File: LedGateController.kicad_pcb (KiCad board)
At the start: 2 copper layers, 49 parts, among them J1 GPIO, J2 SWD, J3 LED_OUT, Q1 FS8205A, Q2 AO3400A, Q3 AO3401A, SW1 BUTTON, SW2 ON_OFF, U1 STM32F030F4Px, U2 MT3608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

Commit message: nearly done
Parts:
- added ?: MountingHole_3.2mm_M3_ISO7380, MountingHole:MountingHole_3.2mm_M3_ISO7380, F.Cu at (161.8, 23.2)
- added ?: MountingHole_3.2mm_M3_ISO7380, MountingHole:MountingHole_3.2mm_M3_ISO7380, F.Cu at (23.2, 41.8)
- added ?: MountingHole_3.2mm_M3_ISO7380, MountingHole:MountingHole_3.2mm_M3_ISO7380, F.Cu at (23.2, 23.2)
- J1: footprint Connector_PinHeader_2.54mm:PinHeader_1x10_P2.54mm_Vertical -> Connector_PinHeader_2.54mm:PinHeader_1x06_P2.54mm_Vertical
- SW1: footprint Button_Switch_THT:SW_PUSH_6mm -> LedGateController:TS-1009B-04326
- SW2: footprint Button_Switch_THT:SW_CuK_OS102011MA1QN1_SPDT_Angled -> SamacSys_Parts:SK12D07VG4NSPA
- TP1, TP2, TP3, TP4, TP5, TP6, TP7: footprint TestPoint:TestPoint_THTPad_D2.0mm_Drill1.0mm -> TestPoint:TestPoint_THTPad_D1.5mm_Drill0.7mm
- moved SW2 90.7 mm to (117.0, 22.2), turned to 180 degrees
- moved C2 89.6 mm to (128.2, 29.6), turned to 90 degrees
- moved U2 82.0 mm to (129.0, 33.9), turned to 90 degrees
- moved R2 80.4 mm to (145.6, 31.6), turned to 270 degrees
- moved C3 80.0 mm to (143.8, 27.2), turned to 90 degrees
- moved C8 76.3 mm to (139.7, 27.2), turned to 90 degrees
- moved R10 75.0 mm to (134.2, 26.3)
- moved C7 74.9 mm to (141.7, 27.3), turned to 90 degrees
- moved D2 74.7 mm to (117.9, 26.6), turned to 0 degrees
- moved R7 74.4 mm to (107.2, 26.1), turned to 90 degrees
- moved Q3 72.5 mm to (109.9, 27.3)
- moved R9 72.0 mm to (131.3, 25.4), turned to 0 degrees
- moved L1 71.2 mm to (121.7, 33.5), turned to 270 degrees
- moved R8 70.8 mm to (121.6, 26.6), turned to 180 degrees
- moved TP7 69.4 mm to (133.5, 29.9)
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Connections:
- J1 pad 1: /PA3 -> GND
- J1 pad 2: /PA4 -> /PA2
- J1 pad 3: /PA5 -> /PA1
- J1 pad 4: /PA6 -> /PA5
- J1 pad 5: /PA7 -> /PA6
- J1 pad 6: /PA10 -> +3V3
- U1 pad 10: /PA4 -> /BATT_ADC
- U1 pad 13: /PA7 -> Net-(U1-Pad13)
- U1 pad 17: /LED_DATA_3V3 -> Net-(U1-Pad17)
- U1 pad 18: /PA10 -> /LED_DATA_3V3
- U1 pad 6: /BATT_ADC -> /LED_EN
- U1 pad 7: /BUTTON -> /PA1
- U1 pad 8: /LED_EN -> /PA2
- U1 pad 9: /PA3 -> /BUTTON
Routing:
- net +BATT: track 0.00 -> 86.1 mm
- net +3V3: track 0.00 -> 83.3 mm, vias 0 -> 4
- net +5V: track 0.00 -> 56.5 mm
- net GND: track 0.00 -> 41.3 mm, vias 0 -> 37
- net +BATT_SW: track 0.00 -> 29.5 mm
- net Net-(BT1-Pad2): track 0.00 -> 27.2 mm
- net /LED_EN: track 0.00 -> 27.2 mm, vias 0 -> 2
- net /LED_DATA_3V3: track 0.00 -> 25.0 mm, vias 0 -> 2
- net /BUTTON: track 0.00 -> 19.0 mm
- net /SWDCLK: track 0.00 -> 19.0 mm, vias 0 -> 1
- net /SWDIO: track 0.00 -> 18.1 mm, vias 0 -> 1
- net /PA5: track 0.00 -> 17.2 mm, vias 0 -> 1
- net /LED_DATA_5V: track 0.00 -> 16.6 mm, vias 0 -> 1
- net /PA6: track 0.00 -> 16.3 mm, vias 0 -> 1
- net /PA2: track 0.00 -> 16.1 mm, vias 0 -> 1
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- added copper zone on F.Cu, net +5V
- added copper zone on F.Cu, net +BATT
- added copper zone on F.Cu, net +BATT_SW
- added copper zone on B.Cu, net GND
- added copper zone on F.Cu, net GND
- added copper zone on F.Cu, net Net-(BT1-Pad2)
- added copper zone on F.Cu, net Net-(D1-Pad2)
- added copper zone on F.Cu, net Net-(Q1-Pad1)
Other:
- board outline added: 145 x 25 mm
- net class Default: clearance 0.2 -> 0.15; via_drill 0.4 -> 0.6
- net class Power (Main) added: clearance 0.15, trace_width 2, via_dia 2, via_drill 1.7
- rule trace_clearance: 0.2 -> 0.15
- rule trace_min: 0.2 -> 0.15
- rule via_min_drill: 0.3 -> 0.35
- rule via_min_size: 0.4 -> 0.7

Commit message: Rev. 1 nearly ready!
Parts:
- moved R6 14.8 mm to (150.5, 28.0), turned to 0 degrees
- moved Q2 11.2 mm to (150.4, 30.8)
- moved R4 8.55 mm to (132.8, 34.8), turned to 180 degrees
- moved R3 7.12 mm to (132.8, 32.8), turned to 180 degrees
- moved R9 6.03 mm to (125.5, 26.6)
- moved R10 4.99 mm to (129.2, 26.6), turned to 0 degrees
- moved C12 4.56 mm to (157.0, 29.5)
- moved C14 4.55 mm to (157.0, 31.5)
- moved U5 4.27 mm to (160.8, 32.0)
- moved TP6 3.80 mm to (163.4, 27.9)
- moved TP5 2.84 mm to (160.4, 27.6)
- moved C11 2.82 mm to (133.9, 40.5), turned to 270 degrees
- moved TP3 2.48 mm to (132.1, 37.2)
- moved C10 2.04 mm to (128.3, 40.5)
- moved U4 1.90 mm to (131.1, 40.6)
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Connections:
- J1 pad 2: /PA2 -> +3V3
- J1 pad 3: /PA1 -> /PA2
- J1 pad 4: /PA5 -> /PA1
- J1 pad 5: /PA6 -> /PA5
- J1 pad 6: +3V3 -> /PA6
- J2 pad 2: /NRST -> +3V3
- J2 pad 3: /SWDIO -> /NRST
- J2 pad 4: /SWDCLK -> /SWDIO
- J2 pad 5: +3V3 -> /SWDCLK
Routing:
- net GND: track 41.3 -> 17.8 mm, vias 37 -> 27
- net +BATT_SW: track 29.5 -> 12.2 mm
- net /LED_EN: track 27.2 -> 13.9 mm
- net /LED_DATA_3V3: track 25.0 -> 32.5 mm, vias 2 -> 1
- net /SWDCLK: track 19.0 -> 24.0 mm
- net /SWDIO: track 18.1 -> 22.9 mm
- net Net-(R3-Pad1): track 11.6 -> 7.43 mm, vias 2 -> 0
- net /BATT_ADC: track 12.1 -> 15.7 mm, vias 0 -> 1
- net /BUTTON: track 19.0 -> 16.7 mm, vias 0 -> 1
- net +5V: track 56.5 -> 58.8 mm, vias 0 -> 3
- net /PA2: track 16.1 -> 14.1 mm
- net /PA6: track 16.3 -> 17.6 mm
- net Net-(C13-Pad2): track 11.7 -> 12.9 mm
- net /PA1: track 14.1 -> 13.1 mm
- net Net-(Q2-Pad1): track 2.68 -> 1.88 mm
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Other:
- board size 145 x 25 mm -> 144.5 x 25 mm
- rule pad_to_mask_clearance: 0.051 -> 0.0508
- board text added: "3V3"
- board text added: "5V (<1A)"
- board text added: "CLK"
- board text added: "DATA"
- board text added: "GND"
- board text added: "IO"
- board text added: "JLCJLCJLCJLC"
- board text added: "NRST"
- board text added: "PA1"
- board text added: "PA2"
- board text added: "PA5"
- board text added: "PA6"
- board text added: "WS28xx LED Driver Rev. 1 github.com/knifa"

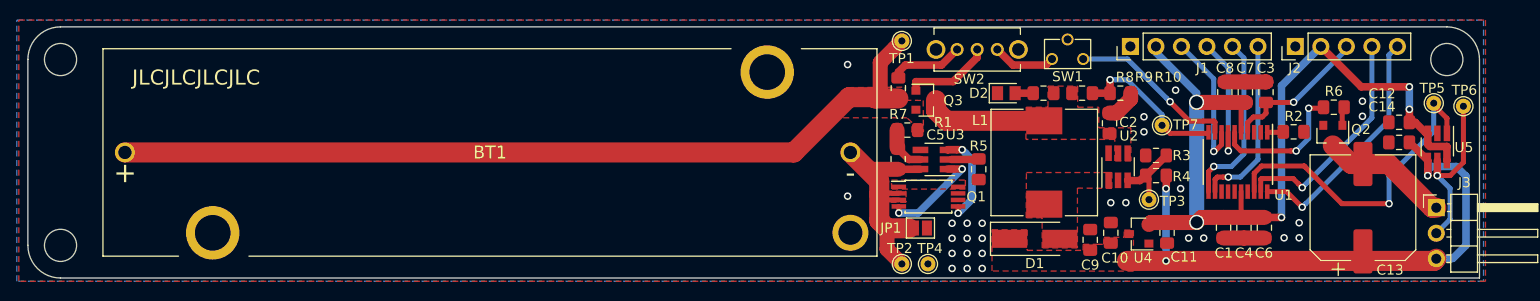
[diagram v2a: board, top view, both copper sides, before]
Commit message: Fix inductor schematic
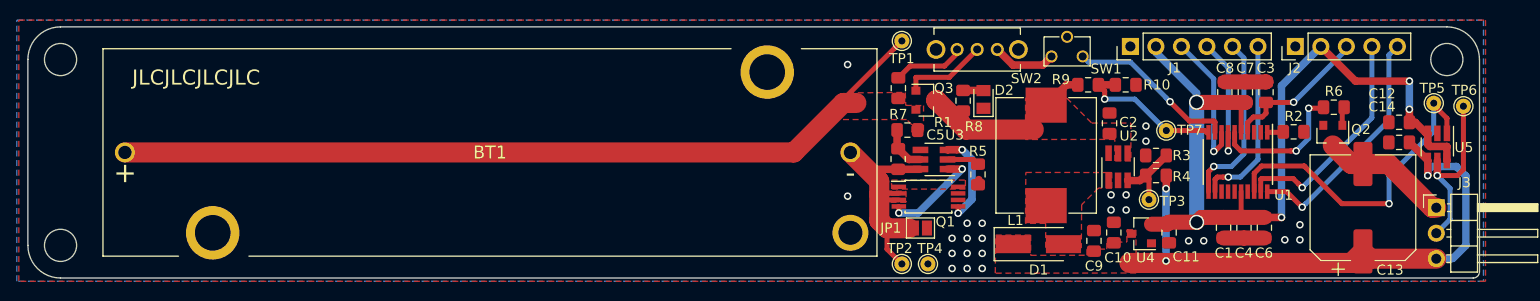
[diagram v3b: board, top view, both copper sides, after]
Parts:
- L1: footprint Inductor_SMD:L_10.4x10.4_H4.8 -> LedGateController:YT1040-220M
- moved R8 8.04 mm to (113.6, 27.4), turned to 90 degrees
- moved D2 2.36 mm to (115.6, 27.2), turned to 90 degrees
- moved R9 1.02 mm to (126.0, 25.8)
- moved R10 0.98 mm to (129.8, 25.8)
- moved L1 0.73 mm to (121.9, 32.8)
- moved TP7 0.68 mm to (133.8, 30.3)
- moved D1 0.64 mm to (121.1, 41.6)
- moved R5 0.52 mm to (115.1, 34.7)
- moved C9 0.39 mm to (126.6, 41.3)
- moved C10 0.30 mm to (128.6, 40.5)
- moved SW1 0.26 mm to (124.0, 22.2)
- moved U4 0.26 mm to (131.3, 40.6)
- moved C11 0.20 mm to (134.1, 40.5)
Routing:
- net +BATT_SW: track 12.2 -> 16.9 mm
- net GND: track 17.8 -> 15.1 mm, vias 27 -> 24
- net +BATT: track 86.1 -> 83.4 mm
- net /BATT_ADC: track 15.7 -> 15.0 mm
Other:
- outline, holes or cut-outs redrawn
- board text added: "5V"
- board text removed: "5V (<1A)"

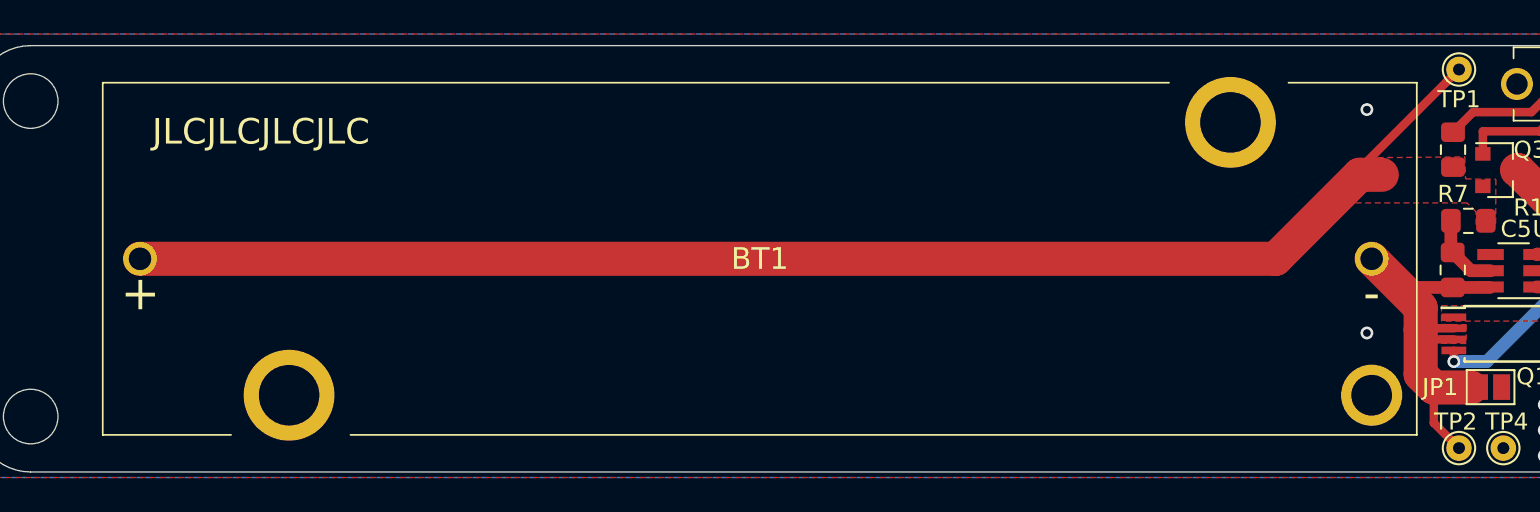
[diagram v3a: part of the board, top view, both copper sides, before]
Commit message: Fix battery orientation
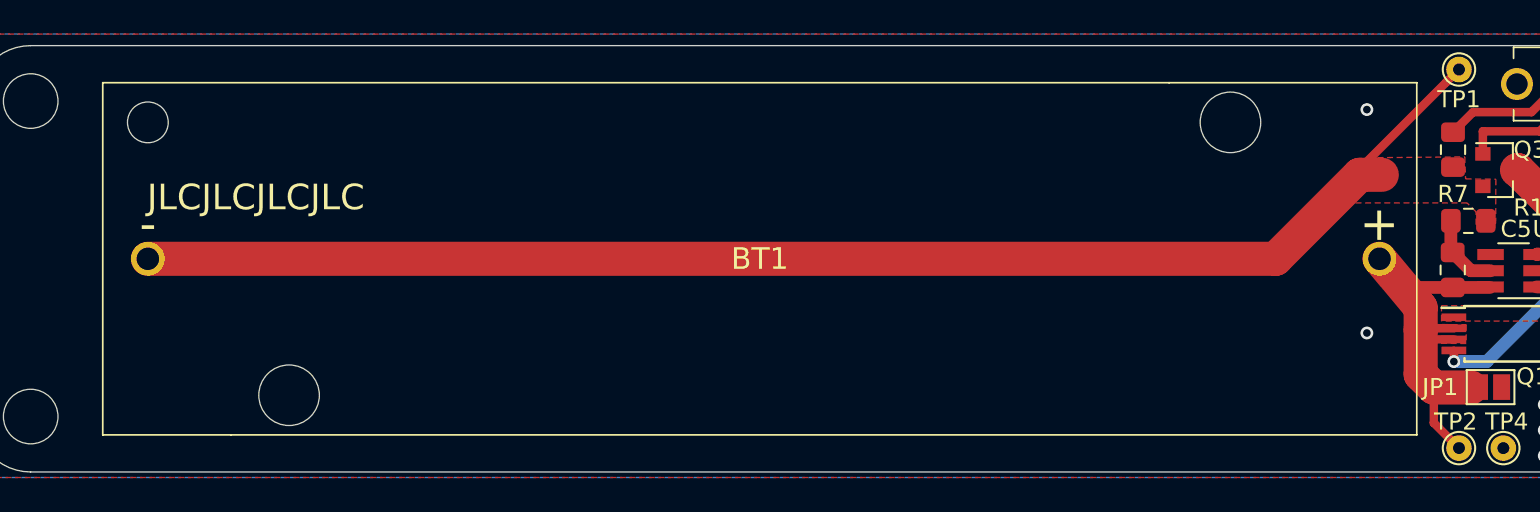
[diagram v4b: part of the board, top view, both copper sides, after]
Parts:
- turned BT1 to 180 degrees
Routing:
- net Net-(BT1-Pad2): track 27.2 -> 24.5 mm
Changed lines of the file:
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@@
     (thickness 1.6)
     (drawings 24)
-    (tracks 300)
+    (tracks 299)
     (zones 0)
     (modules 52)
@@
   )
   (setup
-    (last_trace_width 0.75)
+    (last_trace_width 0.25)
     (user_trace_width 0.5)
     (user_trace_width 0.75)
@@
     (add_net "Net-(C13-Pad2)")
   )
+  (module SamacSys_Parts:1043P (layer F.Cu)
+    (at 66.5 32.5 180)
+    (descr 1043P)
+    (tags "Undefined or Miscellaneous")
+    (fp_text reference BT1 (at 0 0) (layer F.SilkS)
+      (effects (font (size 1.27 1.27) (thickness 0.254)))
+    )
+    (fp_text value LI_ON (at 0 0) (layer F.SilkS) hide
+      (effects (font (size 1 1) (thickness 0.15)))
+    )
+    (fp_line (start 38.525 10.325) (end -24 10.325) (layer F.SilkS) (width 0.1))
+    (fp_line (start 38.525 -10.325) (end 38.525 10.325) (layer F.SilkS) (width 0.1))
+    (fp_line (start 31 -10.325) (end 38.525 -10.325) (layer F.SilkS) (width 0.1))
+    (fp_line (start -38.525 -10.325) (end 31 -10.325) (layer F.SilkS) (width 0.1))
+    (fp_line (start -38.525 10.325) (end -38.525 -10.325) (layer F.SilkS) (width 0.1))
+    (fp_line (start -24 10.325) (end -38.525 10.325) (layer F.SilkS) (width 0.1))
+    (fp_line (start -39.525 11.662) (end -39.525 -11.662) (layer F.CrtYd) (width 0.1))
+    (fp_line (start 39.525 11.662) (end -39.525 11.662) (layer F.CrtYd) (width 0.1))
+    (fp_line (start 39.525 -11.662) (end 39.525 11.662) (layer F.CrtYd) (width 0.1))
+    (fp_line (start -39.525 -11.662) (end 39.525 -11.662) (layer F.CrtYd) (width 0.1))
+    (fp_line (start -38.525 10.325) (end -38.525 -10.325) (layer F.Fab) (width 0.2))
+    (fp_line (start 38.525 10.325) (end -38.525 10.325) (layer F.Fab) (width 0.2))
+    (fp_line (start 38.525 -10.325) (end 38.525 10.325) (layer F.Fab) (width 0.2))
+    (fp_line (start -38.525 -10.325) (end 38.525 -10.325) (layer F.Fab) (width 0.2))
+    (fp_text user %R (at 0 0) (layer F.Fab)
+      (effects (font (size 1.27 1.27) (thickness 0.254)))
+    )
+    (fp_text user + (at -36.322 2.032 180) (layer F.SilkS)
+      (effects (font (size 2 2) (thickness 0.3)))
+    )
+    (fp_text user - (at 35.8775 2.032 180) (layer F.SilkS)
+      (effects (font (size 2 2) (thickness 0.3)))
+    )
+    (pad "" np_thru_hole circle (at -27.6 8 180) (size 3.55 3.55) (drill 3.55) (layers *.Cu *.Mask))
+    (pad "" np_thru_hole circle (at 35.88 8 180) (size 2.39 2.39) (drill 2.39) (layers *.Cu *.Mask))
+    (pad "" np_thru_hole circle (at 27.6 -8 180) (size 3.55 3.55) (drill 3.55) (layers *.Cu *.Mask))
+    (pad 1 thru_hole circle (at 35.88 0 180) (size 1.98 1.98) (drill 1.32) (layers *.Cu *.Mask)
+      (net 1 +BATT))
+    (pad 2 thru_hole circle (at -36.34 0 180) (size 1.98 1.98) (drill 1.32) (layers *.Cu *.Mask)
+      (net 2 "Net-(BT1-Pad2)"))
+    (model D:\Documents\Electronics\LibraryLoaderLibs\SamacSys_Parts.3dshapes\1043P.stp
+      (at (xyz 0 0 0))
+      (scale (xyz 1 1 1))
+      (rotate (xyz 0 0 0))
+    )
+  )
   (module LedGateController:YT1040-220M (layer F.Cu)
     (at 121.865 32.795 270)
@@
     )
     (pad 1 np_thru_hole circle (at 0 0) (size 3.2 3.2) (drill 3.2) (layers *.Cu *.Mask))
-  )
-  (module SamacSys_Parts:1043P (layer F.Cu)
-    (at 66.5 32.5)
-    (descr 1043P)
-    (tags "Undefined or Miscellaneous")
-    (fp_text reference BT1 (at 0 0) (layer F.SilkS)
-      (effects (font (size 1.27 1.27) (thickness 0.254)))
-    )
-    (fp_text value LI_ON (at 0 0) (layer F.SilkS) hide
-      (effects (font (size 1 1) (thickness 0.15)))
-    )
-    (fp_line (start 38.525 10.325) (end -24 10.325) (layer F.SilkS) (width 0.1))
-    (fp_line (start 38.525 -10.325) (end 38.525 10.325) (layer F.SilkS) (width 0.1))
-    (fp_line (start 31 -10.325) (end 38.525 -10.325) (layer F.SilkS) (width 0.1))
-    (fp_line (start -38.525 -10.325) (end 24 -10.325) (layer F.SilkS) (width 0.1))
-    (fp_line (start -38.525 10.325) (end -38.525 -10.325) (layer F.SilkS) (width 0.1))
-    (fp_line (start -31 10.325) (end -38.525 10.325) (layer F.SilkS) (width 0.1))
-    (fp_line (start -39.525 11.662) (end -39.525 -11.662) (layer F.CrtYd) (width 0.1))
-    (fp_line (start 39.525 11.662) (end -39.525 11.662) (layer F.CrtYd) (width 0.1))
-    (fp_line (start 39.525 -11.662) (end 39.525 11.662) (layer F.CrtYd) (width 0.1))
-    (fp_line (start -39.525 -11.662) (end 39.525 -11.662) (layer F.CrtYd) (width 0.1))
-    (fp_line (start -38.525 10.325) (end -38.525 -10.325) (layer F.Fab) (width 0.2))
-    (fp_line (start 38.525 10.325) (end -38.525 10.325) (layer F.Fab) (width 0.2))
-    (fp_line (start 38.525 -10.325) (end 38.525 10.325) (layer F.Fab) (width 0.2))
-    (fp_line (start -38.525 -10.325) (end 38.525 -10.325) (layer F.Fab) (width 0.2))
-    (fp_text user %R (at 0 0) (layer F.Fab)
-      (effects (font (size 1.27 1.27) (thickness 0.254)))
-    )
-    (fp_text user + (at -36.322 2.032) (layer F.SilkS)
-      (effects (font (size 2 2) (thickness 0.3)))
-    )
-    (fp_text user - (at 35.8775 2.032) (layer F.SilkS)
-      (effects (font (size 2 2) (thickness 0.3)))
-    )
-    (pad 5 thru_hole circle (at -27.6 8) (size 5.325 5.325) (drill 3.55) (layers *.Cu *.Mask))
-    (pad 4 thru_hole circle (at 35.88 8) (size 3.585 3.585) (drill 2.39) (layers *.Cu *.Mask))
-    (pad 3 thru_hole circle (at 27.6 -8) (size 5.325 5.325) (drill 3.55) (layers *.Cu *.Mask))
-    (pad 2 thru_hole circle (at 35.88 0) (size 1.98 1.98) (drill 1.32) (layers *.Cu *.Mask)
-      (net 2 "Net-(BT1-Pad2)"))
-    (pad 1 thru_hole circle (at -36.34 0) (size 1.98 1.98) (drill 1.32) (layers *.Cu *.Mask)
-      (net 1 +BATT))
-    (model D:\Documents\Electronics\LibraryLoaderLibs\SamacSys_Parts.3dshapes\1043P.stp
-      (at (xyz 0 0 0))
-      (scale (xyz 1 1 1))
-      (rotate (xyz 0 0 0))
-    )
   )
   (module Capacitor_SMD:C_0805_2012Metric_Pad1.15x1.40mm_HandSolder (layer F.Cu)
@@
   )
   (gr_arc (start 164.375 44.375) (end 164.375 45) (angle -90) (layer Edge.Cuts) (width 0.05))
-  (gr_text JLCJLCJLCJLC (at 37.25 25.05) (layer F.SilkS)
+  (gr_text JLCJLCJLCJLC (at 36.95 28.9) (layer F.SilkS)
     (effects (font (size 1.5 1.5) (thickness 0.3)))
   )
@@
   (gr_line (start 20.5 23.25) (end 20.5 41.75) (layer Edge.Cuts) (width 0.05))
   (segment (start 101.675 27.575) (end 102.975 27.575) (width 2) (layer F.Cu) (net 1))
-  (segment (start 30.16 32.5) (end 96.75 32.5) (width 2) (layer F.Cu) (net 1))
-  (segment (start 96.75 32.5) (end 101.675 27.575) (width 2) (layer F.Cu) (net 1))
   (segment (start 106.750001 22.149999) (end 107.5 21.4) (width 0.5) (layer F.Cu) (net 1))
   (segment (start 101.675 27.575) (end 101.675 27.225) (width 0.5) (layer F.Cu) (net 1))
   (segment (start 101.675 27.225) (end 106.750001 22.149999) (width 0.5) (layer F.Cu) (net 1))
+  (segment (start 96.75 32.5) (end 101.675 27.575) (width 2) (layer F.Cu) (net 1))
+  (segment (start 30.62 32.5) (end 96.75 32.5) (width 2) (layer F.Cu) (net 1))
   (segment (start 107.13169 34.179189) (end 109.320811 34.179189) (width 0.75) (layer F.Cu) (net 2))
-  (segment (start 104.059189 34.179189) (end 102.38 32.5) (width 1.5) (layer F.Cu) (net 2))
   (segment (start 107.13169 34.179189) (end 104.059189 34.179189) (width 0.75) (layer F.Cu) (net 2))
   (segment (start 106.022992 40.05) (end 106.022992 42.122992) (width 0.5) (layer F.Cu) (net 2))
   (segment (start 106.022992 42.122992) (end 107.5 43.6) (width 0.5) (layer F.Cu) (net 2))
-  (segment (start 102.38 32.5) (end 105.25 35.37) (width 2) (layer F.Cu) (net 2))
   (segment (start 105.25 39.277008) (end 106.022992 40.05) (width 2) (layer F.Cu) (net 2))
   (segment (start 106.022992 40.05) (end 108.2 40.05) (width 2) (layer F.Cu) (net 2))
   (segment (start 105.325 36.575) (end 105.25 36.65) (width 0.5) (layer F.Cu) (net 2))
   (segment (start 107.2 36.575) (end 105.325 36.575) (width 0.5) (layer F.Cu) (net 2))
-  (segment (start 105.25 35.37) (end 105.25 36.65) (width 2) (layer F.Cu) (net 2))
   (segment (start 105.25 36.65) (end 105.25 39.277008) (width 2) (layer F.Cu) (net 2))
   (segment (start 105.825 37.225) (end 105.25 36.65) (width 0.5) (layer F.Cu) (net 2))
   (segment (start 107.2 37.225) (end 105.825 37.225) (width 0.5) (layer F.Cu) (net 2))
+  (segment (start 105.25 35.37) (end 105.25 36.65) (width 2) (layer F.Cu) (net 2))
+  (segment (start 102.84 32.5) (end 105.25 35.37) (width 2) (layer F.Cu) (net 2))
   (segment (start 139.524 38.968) (end 141.556 38.968) (width 1.5) (layer F.Cu) (net 3))
   (segment (start 141.556 38.968) (end 143.588 38.968) (width 1.5) (layer F.Cu) (net 3))
@@
   (via (at 129.825 38.225) (size 0.75) (drill 0.45) (layers F.Cu B.Cu) (net 4))
   (via (at 128.325 38.225) (size 0.75) (drill 0.45) (layers F.Cu B.Cu) (net 4))
+  (segment (start 115.38 28.105) (end 115.625 28.105) (width 0.75) (layer F.Cu) (net 4))
   (segment (start 143.479998 27.525) (end 143.75 27.525) (width 0.5) (layer F.Cu) (net 5))
   (via (at 146.5 27.5) (size 0.75) (drill 0.45) (layers F.Cu B.Cu) (net 5))
@@
   (segment (start 152.25 33.65) (end 153.4 33.65) (width 2) (layer F.Cu) (net 8))
   (segment (start 150.4 31.8) (end 152.25 33.65) (width 2) (layer F.Cu) (net 8))
-  (segment (start 115.38 28.105) (end 115.625 28.105) (width 0.75) (layer F.Cu) (net 4))
   (segment (start 115.605 26.325) (end 115.625 26.345) (width 0.75) (layer F.Cu) (net 10))
   (segment (start 113.6 26.325) (end 115.605 26.325) (width 0.75) (layer F.Cu) (net 10))
